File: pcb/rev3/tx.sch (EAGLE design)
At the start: 54 parts, among them U3 MCP73831T-2ACI/OT, Y1 CRYSTAL-26MHZSMD-3.2X2.5

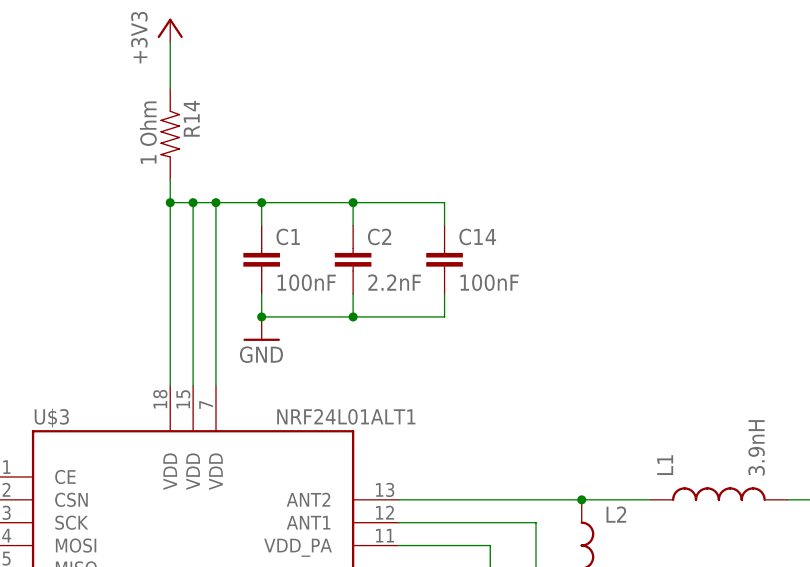
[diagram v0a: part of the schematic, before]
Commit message: tx added mosfet switch
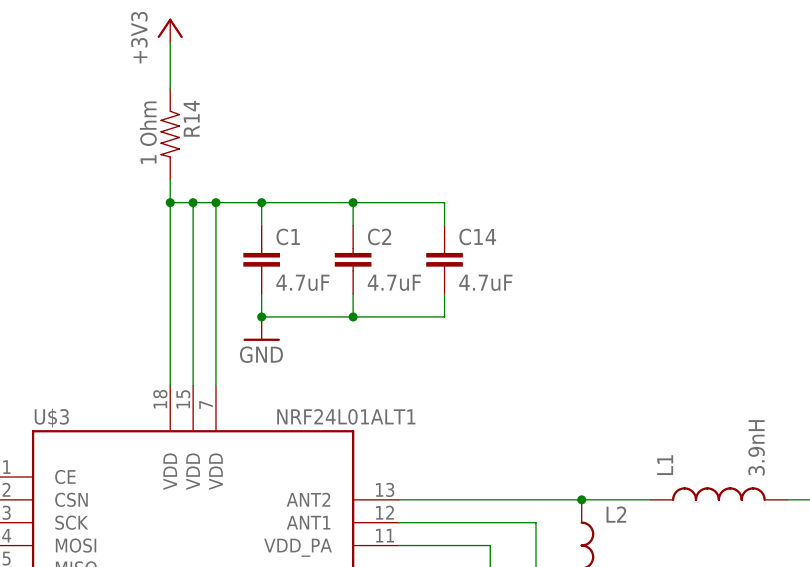
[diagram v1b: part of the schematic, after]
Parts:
- C1, C14: value 100nF -> 4.7uF
- C2: value 2.2nF -> 4.7uF
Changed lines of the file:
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@@
 <part name="+3V1" library="supply1" library_urn="urn:adsk.eagle:library:371" deviceset="+3V3" device=""/>
 <part name="GND1" library="supply1" library_urn="urn:adsk.eagle:library:371" deviceset="GND" device=""/>
-<part name="C1" library="clock" deviceset="CAP" device="0805" value="100nF"/>
+<part name="C1" library="clock" deviceset="CAP" device="0805" value="4.7uF"/>
 <part name="GND12" library="clock" deviceset="GND" device=""/>
 <part name="R1" library="joyAnalog" deviceset="RESISTOR" device="0805-RES" value="22K"/>
-<part name="C2" library="clock" deviceset="CAP" device="0805" value="2.2nF"/>
+<part name="C2" library="clock" deviceset="CAP" device="0805" value="4.7uF"/>
 <part name="C3" library="clock" deviceset="CAP" device="0805" value="100nF"/>
 <part name="GND2" library="clock" deviceset="GND" device=""/>
@@
 <part name="GND21" library="supply1" library_urn="urn:adsk.eagle:library:371" deviceset="GND" device=""/>
 <part name="GND22" library="supply1" library_urn="urn:adsk.eagle:library:371" deviceset="GND" device=""/>
-<part name="C14" library="clock" deviceset="CAP" device="0805" value="100nF"/>
+<part name="C14" library="clock" deviceset="CAP" device="0805" value="4.7uF"/>
 <part name="C15" library="clock" deviceset="CAP" device="0805" value="100nF"/>
 <part name="GND24" library="supply1" library_urn="urn:adsk.eagle:library:371" deviceset="GND" device=""/>
